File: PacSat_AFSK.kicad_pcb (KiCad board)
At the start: 6 copper layers, 92 x 92 mm, 281 parts, among them J2 CONN_02X05, P101 U_FL, P601 U_FL, P651 Conn_04x26_Pin, P702 U_FL, P703 U_FL, Q701 ATF05MS004NT1, U13 AS1016204-0108X0PWAY, U156 AX5043, U2 TMS570LS0914PGE, U205 AX5043, U207 TPS22929D, U28 MAX31331TETB+, U305 AX5043, U307 TPS22929D, U405 AX5043, U406 TPS22929D, U505 AX5043, U506 TPS22929D, U604 RBP-140+, U652 CDCLVC1106, U701 RFShield_OnePiece, U87 QPL9547, U89 TPS22917DBV, U90 STWD100NYWY3F, U91 MAX4495ALAUT, U92 MAX4495ALAUT, U93 MAX4495ALAUT, U94 MAX4495ALAUT, U95 STWD100NYWY3F, U96 TPSM828302ARDSR, U97 LP3962EMP-3.3/NOPB, Y26 32.768kHz, Y601 O 16,0-JT22CT-A-P-3,3-LF

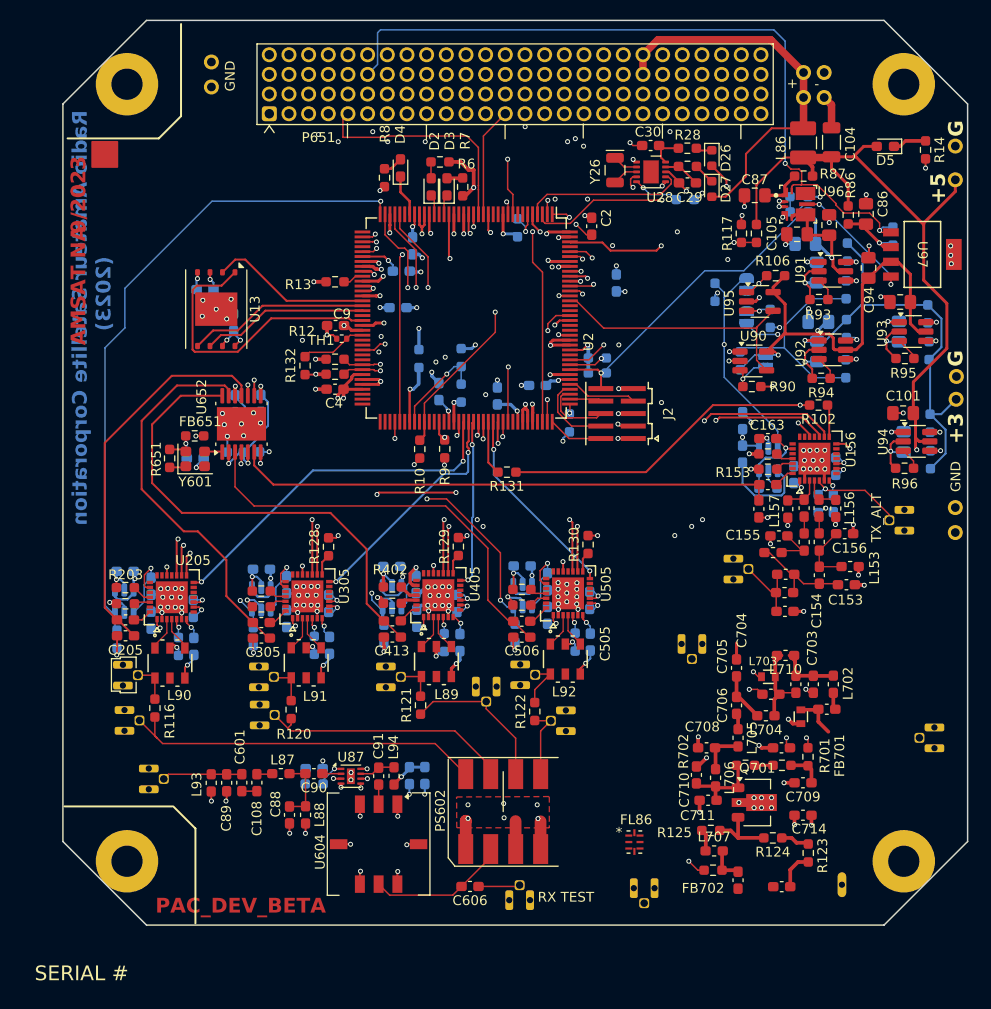
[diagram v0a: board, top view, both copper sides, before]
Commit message: Finished up the TX PA section.
Signed-off-by: Corey Minyard <corey@minyard.net>
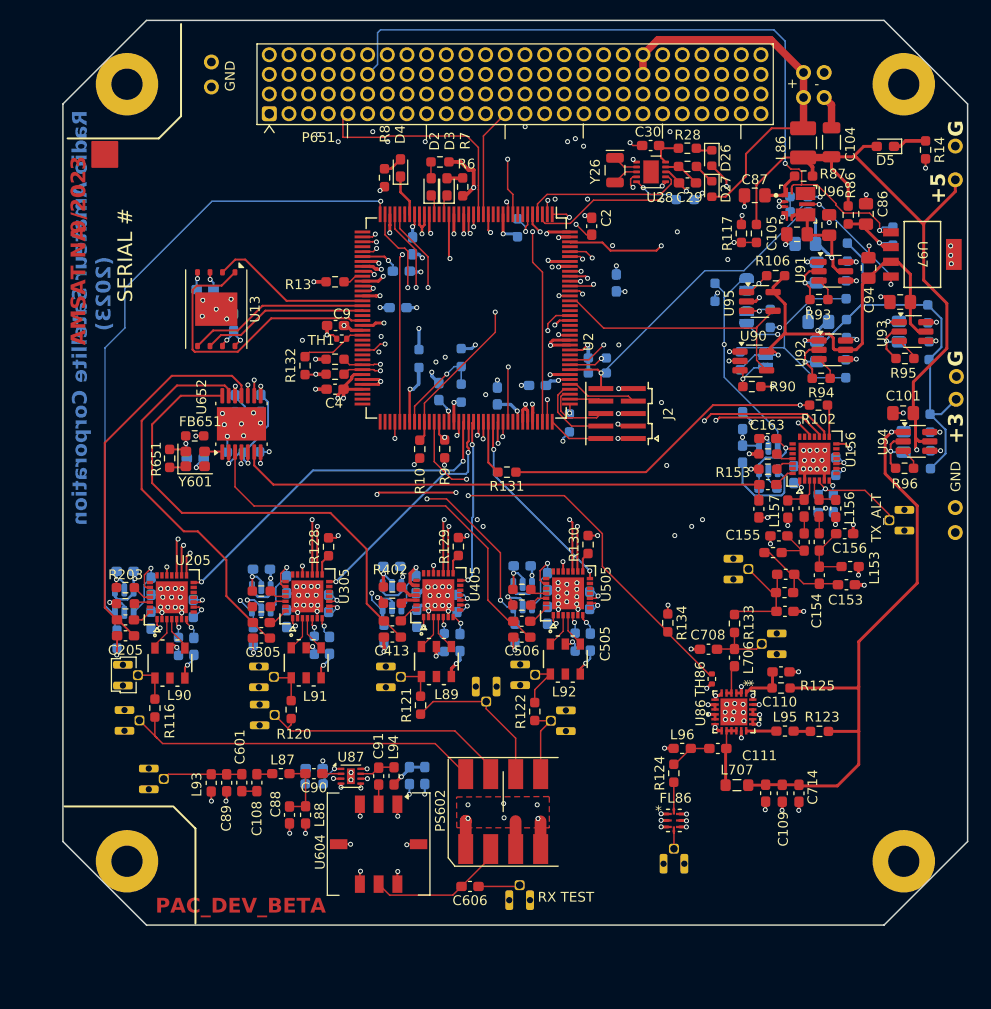
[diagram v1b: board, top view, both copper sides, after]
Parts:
- removed C701, C703: 4p3, Capacitor_SMD:C_0603_1608Metric_Pad1.08x0.95mm_HandSolder
- removed C702: 5p6, Capacitor_SMD:C_0603_1608Metric_Pad1.08x0.95mm_HandSolder
- removed C704: NS, Capacitor_SMD:C_0603_1608Metric_Pad1.08x0.95mm_HandSolder
- removed C705, C717: 2200p, Capacitor_SMD:C_0603_1608Metric_Pad1.08x0.95mm_HandSolder
- removed C706: 18p, Capacitor_SMD:C_0603_1608Metric_Pad1.08x0.95mm_HandSolder
- removed C707: 1u, Capacitor_SMD:C_0603_1608Metric_Pad1.08x0.95mm_HandSolder
- removed C709: 100p, Capacitor_SMD:C_0603_1608Metric_Pad1.08x0.95mm_HandSolder
- removed C710: 56p, Capacitor_SMD:C_0603_1608Metric_Pad1.08x0.95mm_HandSolder
- removed C711: 15p, Capacitor_SMD:C_0603_1608Metric_Pad1.08x0.95mm_HandSolder
- removed FB701, FB702: 2743019447, Resistor_SMD:R_0603_1608Metric_Pad0.98x0.95mm_HandSolder
- removed L701: 100n, PacSatDev_murata:L_0603
- removed L702: 43n, Inductor_SMD:L_0603_1608Metric_Pad1.05x0.95mm_HandSolder
- removed L703: 18n, PacSatDev_murata:L_0603
- removed L704: 1n2, Inductor_SMD:L_0603_1608Metric_Pad1.05x0.95mm_HandSolder
- removed L705: 5n5, Inductor_SMD:L_0603_1608Metric_Pad1.05x0.95mm_HandSolder
- removed L710: 4n7, Inductor_SMD:L_0603_1608Metric_Pad1.05x0.95mm_HandSolder
- removed P702: U_FL, PacSatDev_misc:U_FL
- removed Q701: ATF05MS004NT1, Package_TO_SOT_SMD:SOT-89-3
- removed R701: 50, Resistor_SMD:R_0603_1608Metric_Pad0.98x0.95mm_HandSolder
- removed R702: 0, Resistor_SMD:R_0603_1608Metric_Pad0.98x0.95mm_HandSolder
- removed U701: RFShield_OnePiece, PacSatDev_misc:RF_SHIELD_PAD
- added C109: 1n, Capacitor_SMD:C_0603_1608Metric_Pad1.08x0.95mm_HandSolder, F.Cu at (223.2, 136.6)
- added C110: 100p, Capacitor_SMD:C_0603_1608Metric_Pad1.08x0.95mm_HandSolder, F.Cu at (223.0, 124.2)
- added C111: 60p, Capacitor_SMD:C_0603_1608Metric_Pad1.08x0.95mm_HandSolder, F.Cu at (216.6, 132.0)
- added L95: 68n, Inductor_SMD:L_0603_1608Metric_Pad1.05x0.95mm_HandSolder, F.Cu at (223.4, 130.3)
- added L96: 6.9n, Inductor_SMD:L_0603_1608Metric_Pad1.05x0.95mm_HandSolder, F.Cu at (213.0, 132.0)
- added R133: 0, Resistor_SMD:R_0603_1608Metric_Pad0.98x0.95mm_HandSolder, F.Cu at (218.3, 119.3)
- added R134: 10K 1%, Resistor_SMD:R_0603_1608Metric_Pad0.98x0.95mm_HandSolder, F.Cu at (211.5, 119.3)
- added TH86: NCU15XH103F60RC 10K@25C, Resistor_SMD:R_0402_1005Metric, F.Cu at (216.0, 125.0)
- added U86: TQP7M9106, PacSatDev_misc:QFN24_TQP7M9104_QOR, F.Cu at (218.2, 128.3)
- C708: value 15p -> 37p
- L706: value 5n5 -> 17n
- L707: value 16n6 -> 18n; footprint Inductor_SMD:L_0603_1608Metric_Pad1.05x0.95mm_HandSolder -> Inductor_SMD:L_0805_2012Metric_Pad1.05x1.20mm_HandSolder
- R123: value 0 -> 240
- R125: value 50 -> 240
- R132: value 10K -> 10K 1%
- moved P701 18.7 mm to (222.6, 121.4)
- moved R125 16.2 mm to (223.0, 125.9), turned to 180 degrees
- moved R123 12.4 mm to (226.9, 130.3), turned to 180 degrees
- moved L706 12.4 mm to (218.3, 122.8)
- moved R124 12.0 mm to (212.1, 134.6), turned to 90 degrees
- moved C708 10.0 mm to (215.7, 122.0)
- moved C712 9.28 mm to (221.5, 136.6)
- moved L707 7.08 mm to (218.5, 135.8)
- moved FL86 4.58 mm to (212.1, 139.4)
- moved P703 3.91 mm to (212.1, 143.8), turned to 180 degrees
- moved C714 2.27 mm to (224.8, 136.6), turned to -90 degrees
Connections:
- net CPU_TEMP renamed Net-(U2-AD1IN_16)
- C708 pad 1: Net-(C708-Pad1) -> Net-(P701-In)
- C712 pad 1: Net-(C712-Pad1) -> SSPA_VCC
- L706 pad 1: Net-(C708-Pad1) -> Net-(P701-In)
- L707 pad 1: Net-(L707-Pad1) -> Net-(C111-Pad1)
- L707 pad 2: Net-(C712-Pad1) -> SSPA_VCC
- R123 pad 1: Net-(C717-Pad1) -> SSPA_VCC
- R123 pad 2: Net-(R123-Pad2) -> Net-(L95-Pad2)
- R124 pad 1: Net-(R123-Pad2) -> Net-(FL86-INPUT)
- R124 pad 2: Net-(Q701-D) -> Net-(C111-Pad2)
- R125 pad 1: Net-(L707-Pad1) -> SSPA_VCC
- R125 pad 2: Net-(Q701-D) -> Net-(U86-VBIAS)
- U2 pad 84: unconnected-(U2-AD1IN_23-Pad84) -> PA_TEMP
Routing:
- net SSPA_VCC: track 6.55 -> 62.5 mm, vias 4 -> 1
- net PA_TEMP: track 0.00 -> 44.1 mm, vias 0 -> 2
- net +3.3V: track 115.0 -> 130.2 mm, vias 26 -> 28
- net Net-(C703-Pad2): track 8.56 -> 0.00 mm
- net GND: track 256.9 -> 264.9 mm, vias 217 -> 232
- net Net-(Q701-D): track 6.80 -> 0.00 mm
- net Net-(C111-Pad1): track 0.00 -> 6.57 mm
- net Net-(C702-Pad2): track 6.18 -> 0.00 mm
- net Net-(C705-Pad1): track 5.01 -> 0.00 mm
- net Net-(L706-Pad2): track 8.24 -> 3.35 mm
- net Net-(C708-Pad1): track 4.63 -> 0.00 mm
- net Net-(U86-VBIAS): track 0.00 -> 4.51 mm
- net TX_OUT_DRV: track 7.69 -> 12.1 mm
- net Net-(C111-Pad2): track 0.00 -> 4.41 mm
- net Net-(C717-Pad1): track 4.40 -> 0.00 mm
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
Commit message: Add resistors to the JTAG interface
They are supposed to be there.

Signed-off-by: Corey Minyard <corey@minyard.net>
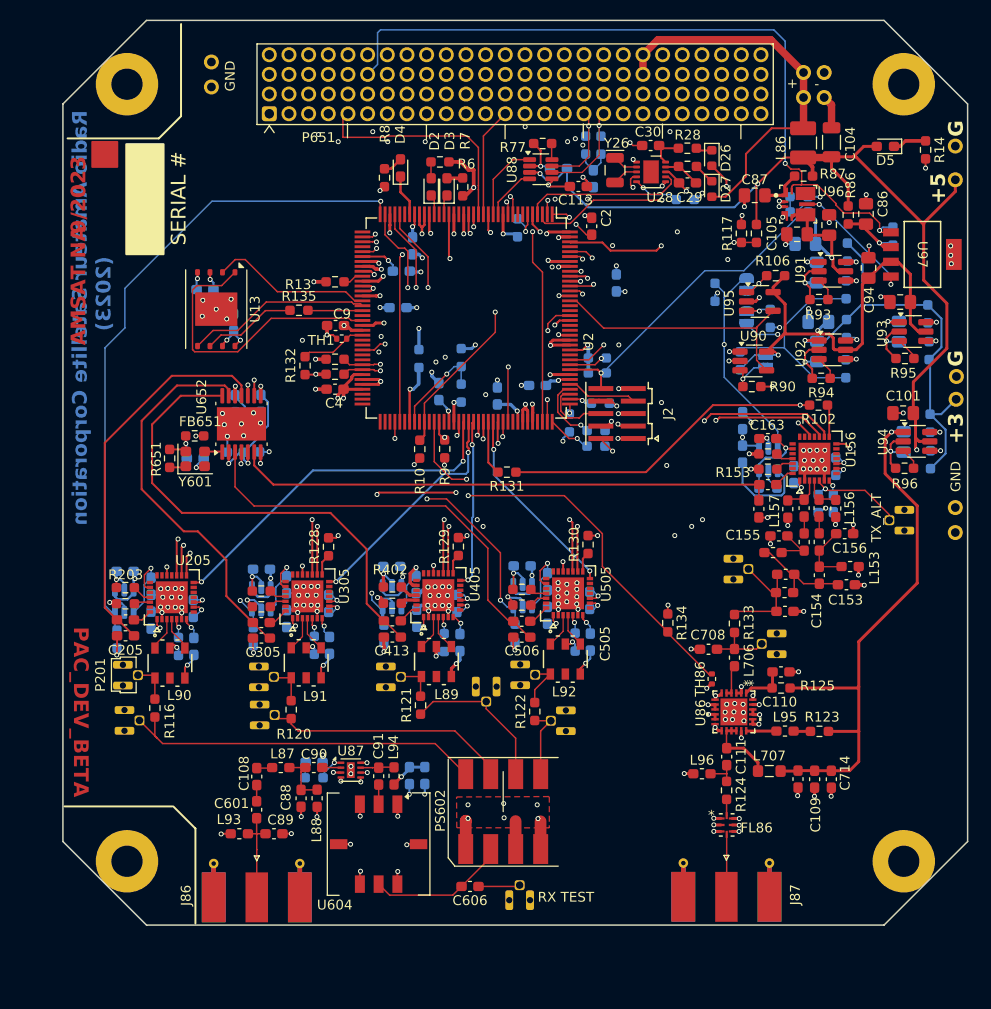
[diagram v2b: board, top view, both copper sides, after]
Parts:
- removed P601, P703: U_FL, PacSatDev_misc:U_FL
- added C112: 100n, Capacitor_SMD:C_0603_1608Metric_Pad1.08x0.95mm_HandSolder, B.Cu at (200.4, 73.1)
- added C113: 100n, Capacitor_SMD:C_0603_1608Metric_Pad1.08x0.95mm_HandSolder, F.Cu at (202.4, 74.9)
- added C114: 4.7nF, Capacitor_SMD:C_0603_1608Metric_Pad1.08x0.95mm_HandSolder, B.Cu at (203.9, 74.1)
- added J86: Conn_Coaxial, Connector_Coaxial:SMA_Molex_73251-1153_EdgeMount_Horizontal, F.Cu at (169.7, 145.5)
- added J87: Conn_Coaxial, Connector_Coaxial:SMA_Molex_73251-1153_EdgeMount_Horizontal, F.Cu at (217.5, 145.4)
- added R135: 33, Resistor_SMD:R_0603_1608Metric_Pad0.98x0.95mm_HandSolder, F.Cu at (174.0, 87.5)
- added R136: 22, Resistor_SMD:R_0603_1608Metric_Pad0.98x0.95mm_HandSolder, B.Cu at (204.2, 99.7)
- added R137: 22, Resistor_SMD:R_0603_1608Metric_Pad0.98x0.95mm_HandSolder, B.Cu at (204.7, 96.9)
- added R138: 22, Resistor_SMD:R_0603_1608Metric_Pad0.98x0.95mm_HandSolder, B.Cu at (204.2, 101.3)
- added R77: 10K, Resistor_SMD:R_0603_1608Metric_Pad0.98x0.95mm_HandSolder, F.Cu at (198.8, 70.5)
- added R79: 61.9Ω, Resistor_SMD:R_0603_1608Metric_Pad0.98x0.95mm_HandSolder, B.Cu at (203.2, 70.7)
- added R80: 61.9Ω, Resistor_SMD:R_0603_1608Metric_Pad0.98x0.95mm_HandSolder, B.Cu at (204.7, 70.7)
- added U88: TCAN1044ADDFRQ1, Package_TO_SOT_SMD:TSOT-23-8, F.Cu at (198.6, 73.1)
- moved C89 7.07 mm to (171.5, 140.7), turned to 180 degrees
- moved L93 5.91 mm to (167.9, 140.7), turned to 180 degrees
- moved R124 5.65 mm to (217.5, 136.3)
- moved FL86 5.39 mm to (217.5, 139.8)
- moved C714 3.59 mm to (228.1, 135.2)
- moved L707 3.59 mm to (221.8, 134.3)
- moved C109 3.59 mm to (226.4, 135.2)
- moved C712 3.59 mm to (224.8, 135.2)
- moved L96 3.27 mm to (215.0, 134.6)
- moved C601 3.14 mm to (169.7, 138.3), turned to -90 degrees
- moved C88 2.06 mm to (174.2, 137.1)
- moved L88 2.06 mm to (175.8, 137.1)
- moved C111 1.23 mm to (217.5, 132.9), turned to -90 degrees
- moved C90 0.62 mm to (175.5, 134.0)
- moved C92 0.62 mm to (175.5, 133.5)
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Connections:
- P651 pad 65: unconnected-(P651-Pin_65-Pad65) -> CAN+
- P651 pad 69: unconnected-(P651-Pin_69-Pad69) -> CAN-
- U13 pad 6: MRAM_CLK -> Net-(U13-SCK)
- U2 pad 108: Net-(J2-P2) -> Net-(U2-TMS)
- U2 pad 110: Net-(J2-P8) -> Net-(U2-TDI)
- U2 pad 112: Net-(J2-P4) -> Net-(U2-TCK)
- U2 pad 12: unconnected-(U2-CAN3RX-Pad12) -> CAN_A_RX
- U2 pad 13: unconnected-(U2-CAN3TX-Pad13) -> CAN_A_TX
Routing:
- net +5V: track 175.8 -> 203.3 mm, vias 2 -> 4
- net MRAM_CLK: track 17.0 -> 5.56 mm
- net CAN-: track 0.00 -> 11.1 mm, vias 0 -> 1
- net CAN+: track 0.00 -> 9.86 mm, vias 0 -> 1
- net Net-(U13-SCK): track 0.00 -> 9.60 mm
- net CAN_A_TX: track 0.00 -> 8.08 mm
- net GND: track 264.9 -> 272.1 mm, vias 232 -> 234
- net Net-(U2-TCK): track 0.00 -> 6.97 mm, vias 0 -> 1
- net Net-(J2-P4): track 8.18 -> 2.49 mm, vias 0 -> 1
- net CAN_A_RX: track 0.00 -> 5.42 mm
- net Net-(U2-TMS): track 0.00 -> 4.57 mm, vias 0 -> 1
- net Net-(FL86-OUTPUT): track 1.93 -> 6.37 mm
- net SSPA_VCC: track 62.5 -> 58.5 mm
- net Net-(C114-Pad1): track 0.00 -> 3.92 mm
- net +3.3V: track 130.2 -> 133.2 mm, vias 28 -> 29
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
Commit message: Clean up tracks on the board
Signed-off-by: Corey Minyard <corey@minyard.net>
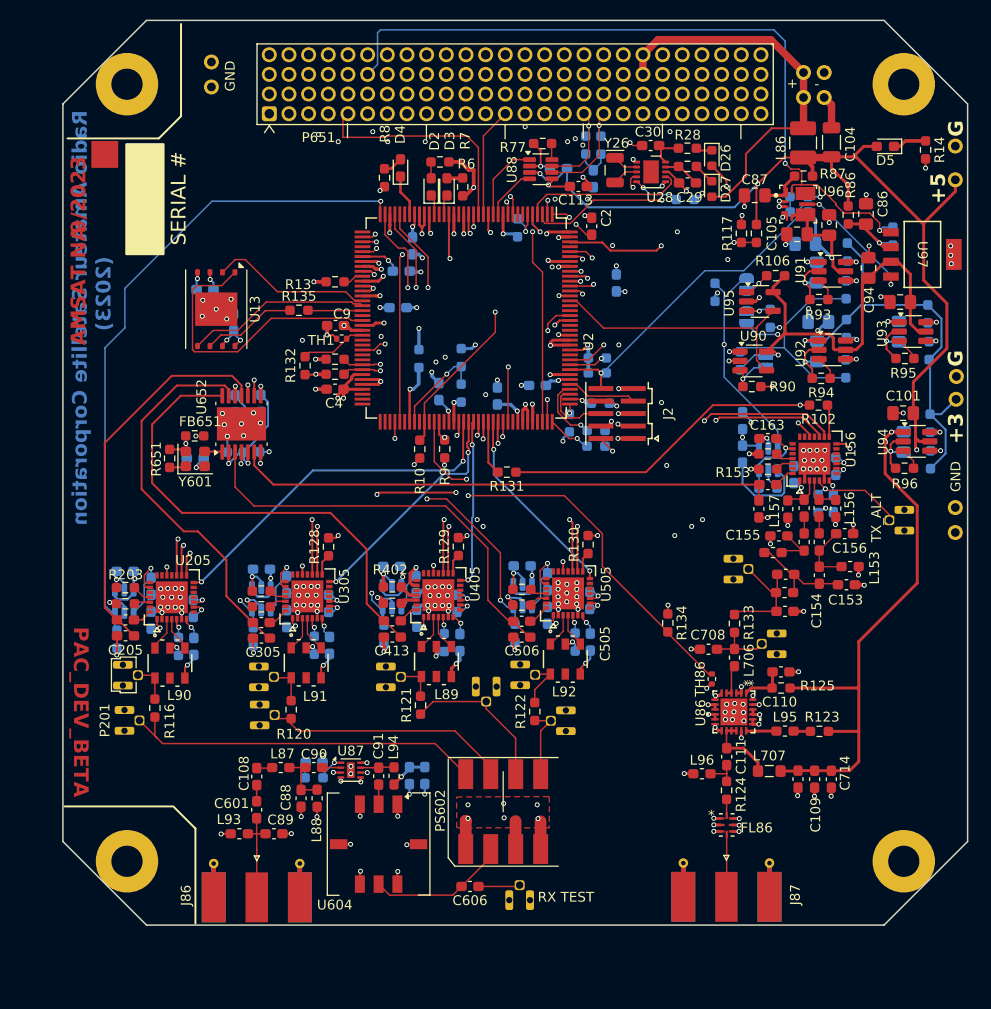
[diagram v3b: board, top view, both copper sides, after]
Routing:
- net GND: track 272.1 -> 262.5 mm
- net +3.3V: track 133.2 -> 131.4 mm
- net TX_OUT_DRV: track 12.1 -> 10.6 mm
- net Net-(J2-P6): track 7.74 -> 6.34 mm
- net Net-(J2-P8): track 2.97 -> 1.58 mm
- net VSYS: track 40.9 -> 39.5 mm
- net Port2_P: track 25.2 -> 23.9 mm
- net CAN+: track 9.86 -> 8.74 mm
- net +5V: track 203.3 -> 202.2 mm
- net REG_1V2: track 16.4 -> 15.4 mm
- net AX5043_3V3: track 115.5 -> 114.5 mm
- net CAN-: track 11.1 -> 10.2 mm
- net Net-(J2-P4): track 2.49 -> 1.59 mm
- net Net-(U95-WDO_N): track 4.29 -> 3.40 mm
- net Net-(U652-1G): track 21.6 -> 20.8 mm
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
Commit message: More cleanups, set the value for the SMA connectors
Signed-off-by: Corey Minyard <corey@minyard.net>
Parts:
- J86, J87: value Conn_Coaxial -> Molex 73251-1153
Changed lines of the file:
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@@
 			)
 		)
-		(property "Value" "Conn_Coaxial"
+		(property "Value" "Molex 73251-1153"
 			(at -1.72 -7.11 90)
 			(layer "F.Fab")
@@
 			)
 		)
-		(property "Value" "Conn_Coaxial"
+		(property "Value" "Molex 73251-1153"
 			(at -1.72 -7.11 90)
 			(layer "F.Fab")
